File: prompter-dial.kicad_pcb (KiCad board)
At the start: 2 copper layers, 75 x 74.2 mm, 8 parts, among them J1 PROMPTER WHEEL, SW1 JUMP_B, SW2 RUN, U1 ATtiny85-20S

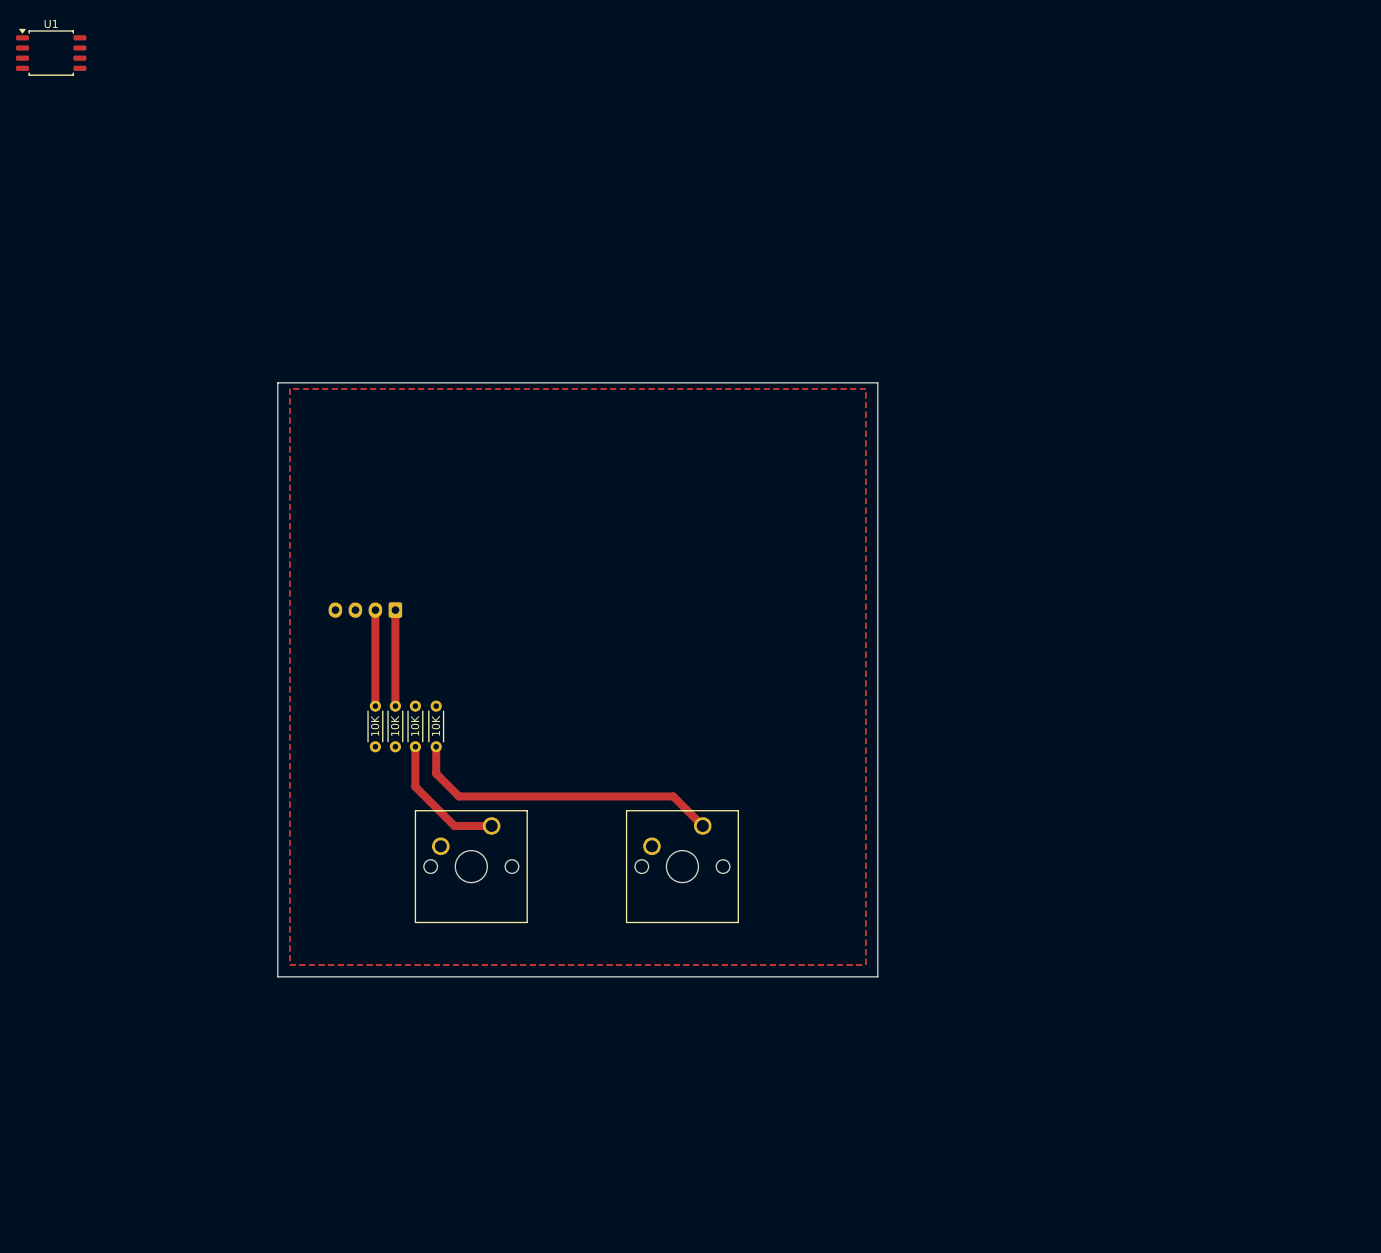
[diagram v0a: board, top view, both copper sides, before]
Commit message: Add drill hole
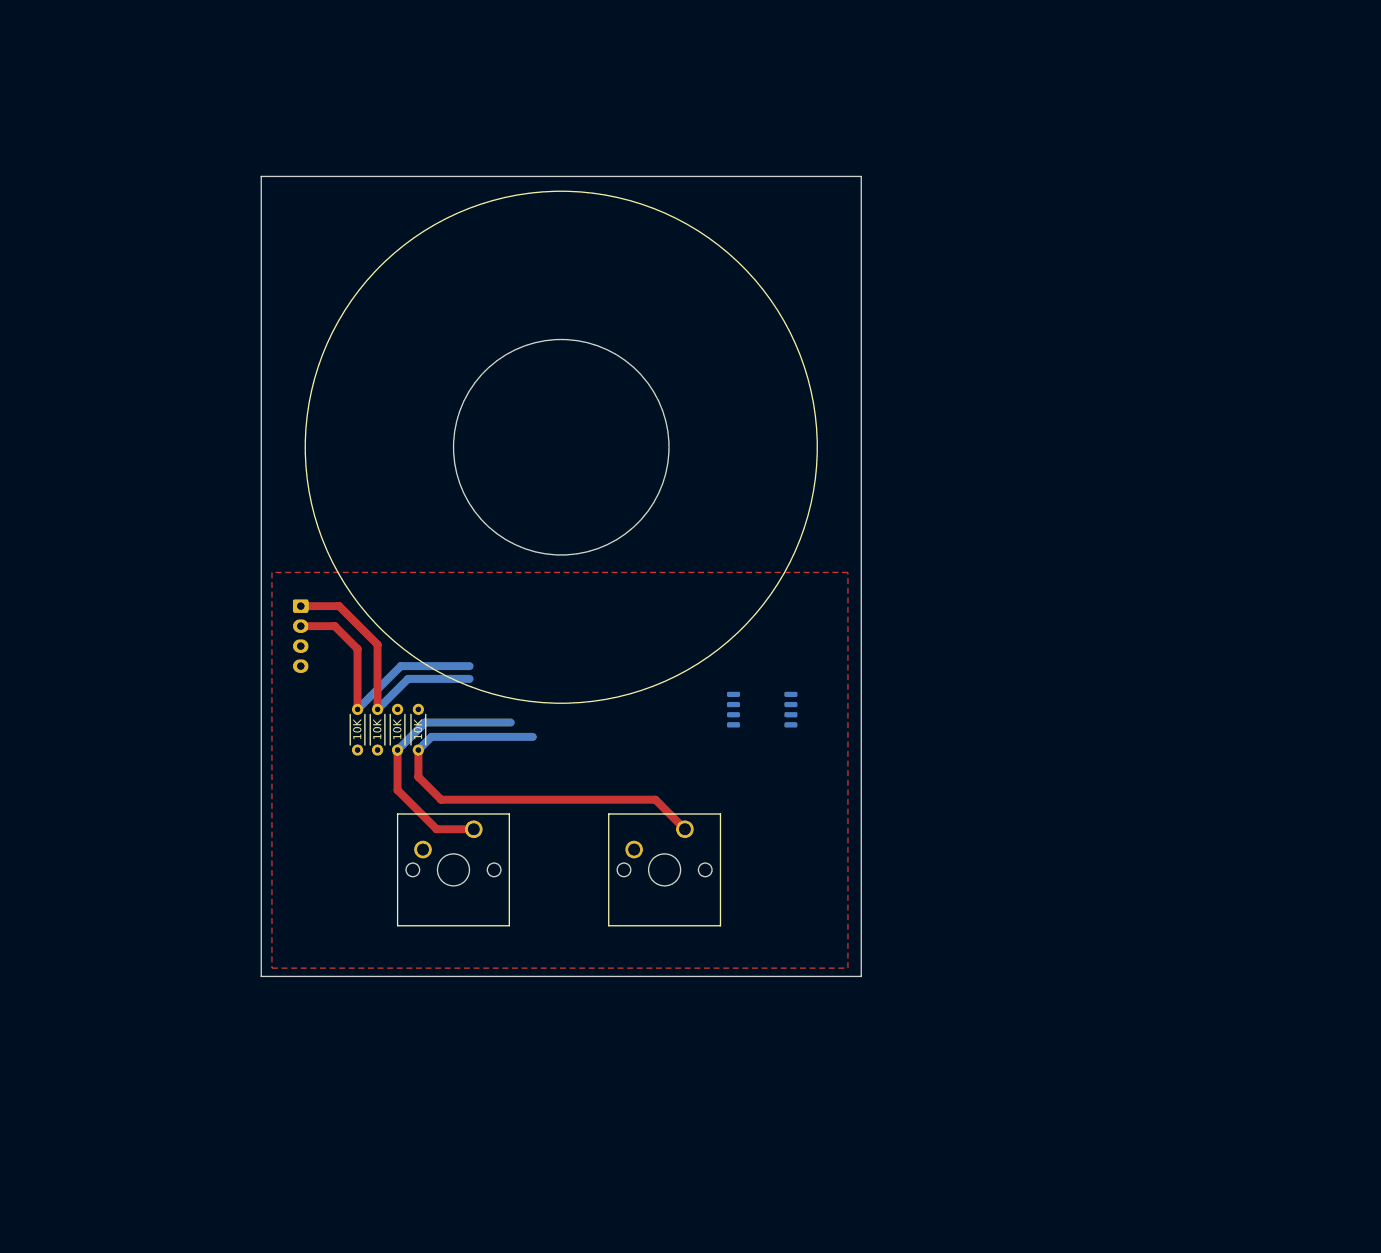
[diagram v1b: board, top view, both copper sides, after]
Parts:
- U1: moved to B.Cu
- moved U1 121.0 mm to (93.5, 85.1), turned to 180 degrees
- moved J1 11.8 mm to (35.9, 72.2), turned to -90 degrees
- moved R1 2.27 mm to (48.0, 90.2)
- moved R5 2.27 mm to (43.0, 90.2)
- moved R6 2.27 mm to (45.5, 90.2)
- moved SW2 2.27 mm to (83.9, 100.0)
- moved R2 2.27 mm to (50.6, 90.2)
- moved SW1 2.27 mm to (57.5, 100.0)
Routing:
- net ENC_A: track 12.0 -> 32.8 mm
- net ENC_B: track 12.0 -> 32.1 mm
- net JUMP_B: track 16.6 -> 32.1 mm
- net RUN: track 39.4 -> 54.4 mm
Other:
- board size 75 x 74.2 mm -> 75 x 100 mm
- board text added: "PROMPTER WHEEL V2.1 CAMERON-MORGAN.COM"

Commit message: Update prompter-dial.kicad_pcb
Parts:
- removed U1: ATtiny85-20S, Package_SO:SOIC-8_5.3x5.3mm_P1.27mm
- SW1: value JUMP_B -> JUMP
- moved J1 133.2 mm to (162.0, 115.0), turned to 90 degrees
- moved R6 116.2 mm to (154.8, 129.5)
- moved R5 115.6 mm to (151.6, 129.5)
- moved R1 107.9 mm to (148.4, 129.5)
- moved R2 102.6 mm to (145.3, 129.5)
- moved SW1 61.0 mm to (110.3, 130.7)
- moved SW2 57.5 mm to (132.6, 130.7)
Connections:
- net JUMP_B renamed JUMP
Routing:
- net RUN: track 54.4 -> 13.1 mm
- net JUMP: track 32.1 -> 68.9 mm
- net ENC_A: track 32.8 -> 14.3 mm
- net ENC_B: track 32.1 -> 18.5 mm
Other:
- board size 75 x 100 mm -> 100 x 110 mm

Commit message: Update prompter-dial.kicad_pcb
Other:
- board text added: "PROMPTER DIAL V2.1 CAMERON-MORGAN.COM"
- board text removed: "PROMPTER WHEEL V2.1 CAMERON-MORGAN.COM"
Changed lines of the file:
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@@
 		)
 	)
-	(gr_text "PROMPTER WHEEL V2.1\nCAMERON-MORGAN.COM"
+	(gr_text "PROMPTER DIAL V2.1\nCAMERON-MORGAN.COM"
 		(at 77.31875 128.8625 90)
 		(layer "B.SilkS")
